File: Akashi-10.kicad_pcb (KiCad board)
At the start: 2 copper layers, 66 x 65 mm, 12 parts, among them J1 Conn_02x20_Odd_Even, P1 EL-210-KEY, U1 9-ST-20

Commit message: Fixed name of the KEY matrix sisgnal.
The Row signal order was up-side-down. Fixed.
The Col signal was 1 origin. Fixed as 0 origin.
Sylscreen modfified.
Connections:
- J1 pad 30: Net-(J1-Pad30) -> unconnected-(J1-Pad30)
- J1 pad 32: Net-(J1-Pad32) -> unconnected-(J1-Pad32)
- J1 pad 34: Net-(J1-Pad34) -> unconnected-(J1-Pad34)
- J1 pad 36: Net-(J1-Pad36) -> unconnected-(J1-Pad36)
- J1 pad 39: Net-(J1-Pad39) -> unconnected-(J1-Pad39)
- J1 pad 4: Net-(J1-Pad4) -> unconnected-(J1-Pad4)
- P1 pad 12: Net-(P1-Pad12) -> unconnected-(P1-Pad12)
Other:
- net class Default removed
- board text added: "Akashi-10 v1.0.3"
- board text removed: "Akashi-10 v1.0.2"

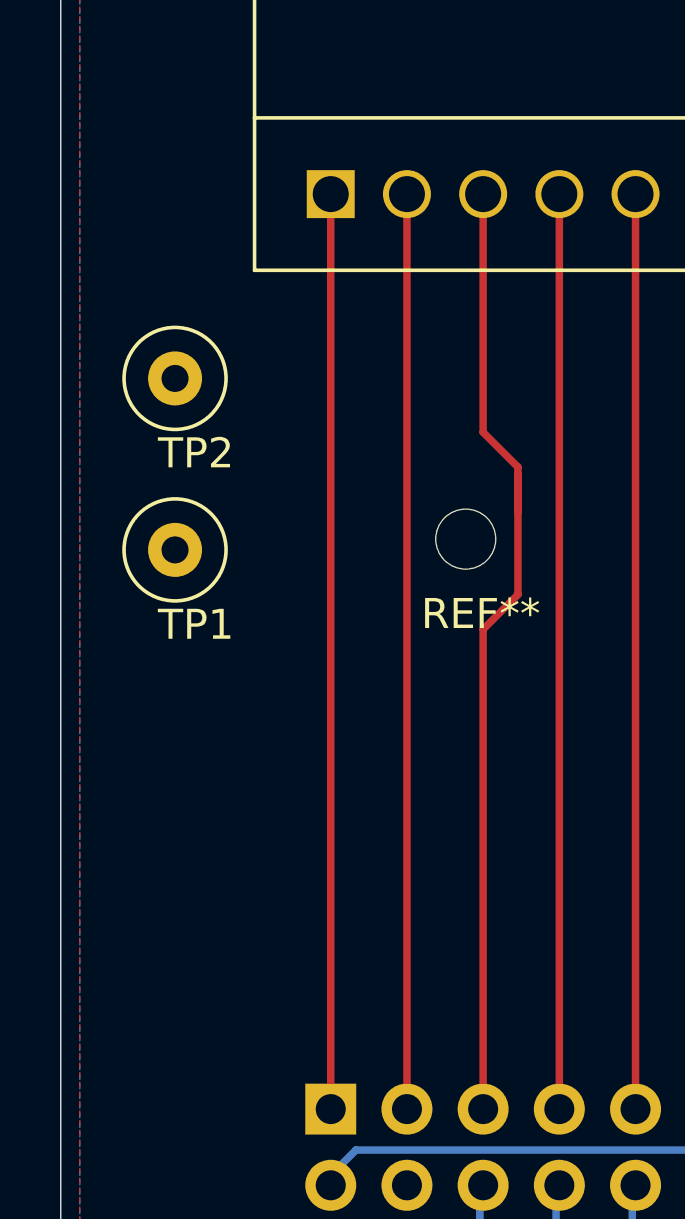
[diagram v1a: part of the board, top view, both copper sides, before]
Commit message: Add pin 1 mark to the connector.
Add pin 1 mark to the connector of the layout.
Movied Testpoint ( 3.3 and GND hole )
Update photo.
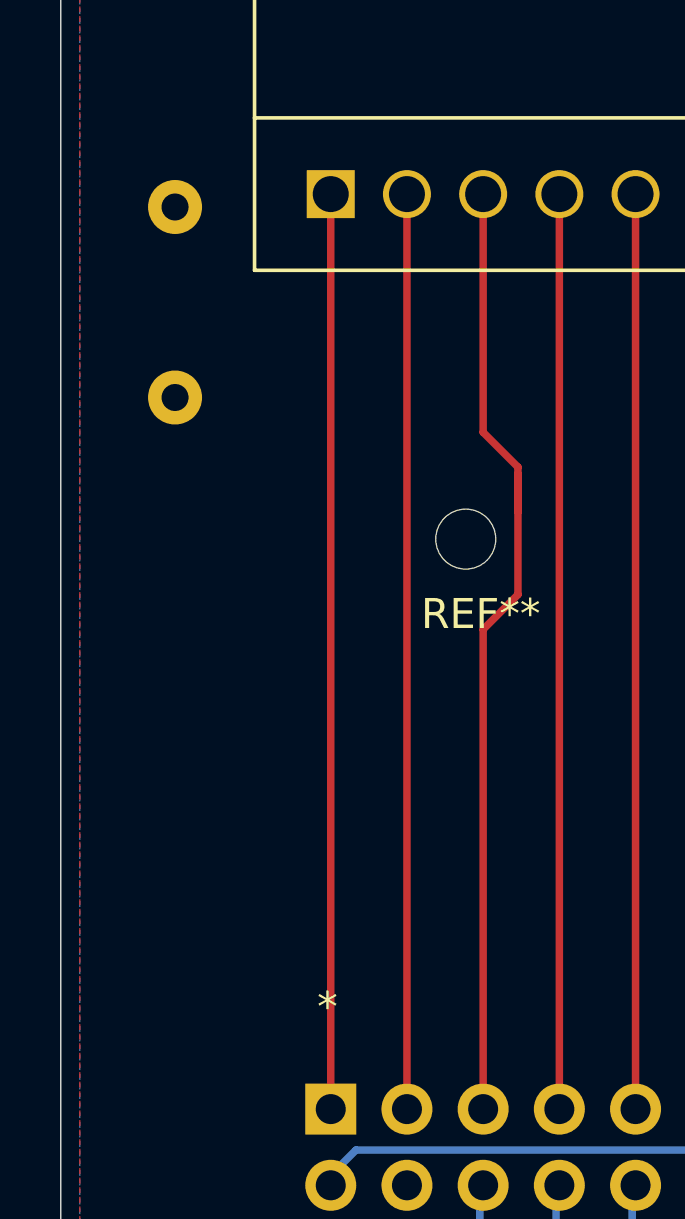
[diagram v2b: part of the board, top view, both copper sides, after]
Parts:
- TP1, TP2: moved to B.Cu
- moved TP2 5.71 mm to (122.8, 85.9), turned to 180 degrees
- moved TP1 5.08 mm to (122.8, 92.3), turned to 180 degrees
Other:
- board text added: "*"
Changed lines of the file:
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@@
       (net 1 "GND") (pinfunction "GND") (pintype "power_in"))
-  )
-  (footprint "TestPoint:TestPoint_Loop_D2.60mm_Drill0.9mm_Beaded" (layer "F.Cu")
-    (at 122.81 97.36)
-    (descr "wire loop with bead as test point, loop diameter2.6mm, hole diameter 0.9mm")
-    (tags "test point wire loop bead")
-    (property "Sheetfile" "Akashi-10.kicad_sch")
-    (property "Sheetname" "")
-    (attr through_hole)
-    (fp_text reference "TP1" (at 0.7 2.5) (layer "F.SilkS")
-      (effects (font (size 1 1) (thickness 0.15)))
-    )
-    (fp_text value "TestPoint" (at 0 -2.8) (layer "F.Fab")
-      (effects (font (size 1 1) (thickness 0.15)))
-    )
-    (fp_text user "${REFERENCE}" (at 0.7 2.5) (layer "F.Fab")
-      (effects (font (size 1 1) (thickness 0.15)))
-    )
-    (fp_circle (center 0 0) (end 1.7 0) (layer "F.SilkS") (width 0.12) (fill none))
-    (fp_circle (center 0 0) (end 2 0) (layer "F.CrtYd") (width 0.05) (fill none))
-    (fp_line (start 1.3 0.3) (end 1.3 -0.3) (layer "F.Fab") (width 0.12))
-    (fp_line (start -1.3 -0.3) (end -1.3 0.3) (layer "F.Fab") (width 0.12))
-    (fp_line (start 1.3 -0.3) (end -1.3 -0.3) (layer "F.Fab") (width 0.12))
-    (fp_line (start -1.3 0.3) (end 1.3 0.3) (layer "F.Fab") (width 0.12))
-    (fp_circle (center 0 0) (end 1.5 0) (layer "F.Fab") (width 0.12) (fill none))
-    (pad "1" thru_hole circle locked (at 0 0) (size 1.8 1.8) (drill 0.9) (layers *.Cu *.Mask)
-      (net 1 "GND") (pinfunction "1") (pintype "passive"))
-    (model "${KISYS3DMOD}/TestPoint.3dshapes/TestPoint_Loop_D2.60mm_Drill0.9mm_Beaded.wrl"
-      (offset (xyz 0 0 0))
-      (scale (xyz 1 1 1))
-      (rotate (xyz 0 0 0))
-    )
-  )
-  (footprint "TestPoint:TestPoint_Loop_D2.60mm_Drill0.9mm_Beaded" (layer "F.Cu")
-    (at 122.81 91.645)
-    (descr "wire loop with bead as test point, loop diameter2.6mm, hole diameter 0.9mm")
-    (tags "test point wire loop bead")
-    (property "Sheetfile" "Akashi-10.kicad_sch")
-    (property "Sheetname" "")
-    (attr through_hole)
-    (fp_text reference "TP2" (at 0.7 2.5) (layer "F.SilkS")
-      (effects (font (size 1 1) (thickness 0.15)))
-    )
-    (fp_text value "TestPoint" (at 0 -2.8) (layer "F.Fab")
-      (effects (font (size 1 1) (thickness 0.15)))
-    )
-    (fp_text user "${REFERENCE}" (at 0.7 2.5) (layer "F.Fab")
-      (effects (font (size 1 1) (thickness 0.15)))
-    )
-    (fp_circle (center 0 0) (end 1.7 0) (layer "F.SilkS") (width 0.12) (fill none))
-    (fp_circle (center 0 0) (end 2 0) (layer "F.CrtYd") (width 0.05) (fill none))
-    (fp_line (start 1.3 -0.3) (end -1.3 -0.3) (layer "F.Fab") (width 0.12))
-    (fp_line (start -1.3 0.3) (end 1.3 0.3) (layer "F.Fab") (width 0.12))
-    (fp_line (start 1.3 0.3) (end 1.3 -0.3) (layer "F.Fab") (width 0.12))
-    (fp_line (start -1.3 -0.3) (end -1.3 0.3) (layer "F.Fab") (width 0.12))
-    (fp_circle (center 0 0) (end 1.5 0) (layer "F.Fab") (width 0.12) (fill none))
-    (pad "1" thru_hole circle locked (at 0 0) (size 1.8 1.8) (drill 0.9) (layers *.Cu *.Mask)
-      (net 3 "+3V3") (pinfunction "1") (pintype "passive"))
-    (model "${KISYS3DMOD}/TestPoint.3dshapes/TestPoint_Loop_D2.60mm_Drill0.9mm_Beaded.wrl"
-      (offset (xyz 0 0 0))
-      (scale (xyz 1 1 1))
-      (rotate (xyz 0 0 0))
-    )
   )
   (footprint "9-ST-20:9-ST-20" (layer "F.Cu")
@@
     )
     (pad "" np_thru_hole circle locked (at 0 0) (size 2.8 2.8) (drill 2.8) (layers *.Cu *.Mask))
+  )
+  (footprint "TestPoint:TestPoint_Loop_D2.60mm_Drill0.9mm_Beaded" (layer "B.Cu")
+    (at 122.81 92.28 180)
+    (descr "wire loop with bead as test point, loop diameter2.6mm, hole diameter 0.9mm")
+    (tags "test point wire loop bead")
+    (property "Sheetfile" "Akashi-10.kicad_sch")
+    (property "Sheetname" "")
+    (attr through_hole)
+    (fp_text reference "TP1" (at 0.7 -2.5) (layer "B.SilkS")
+      (effects (font (size 1 1) (thickness 0.15)) (justify mirror))
+    )
+    (fp_text value "TestPoint" (at 0 2.8) (layer "B.Fab")
+      (effects (font (size 1 1) (thickness 0.15)) (justify mirror))
+    )
+    (fp_text user "${REFERENCE}" (at 0.7 -2.5) (layer "B.Fab")
+      (effects (font (size 1 1) (thickness 0.15)) (justify mirror))
+    )
+    (fp_circle (center 0 0) (end 1.7 0) (layer "B.SilkS") (width 0.12) (fill none))
+    (fp_circle (center 0 0) (end 2 0) (layer "B.CrtYd") (width 0.05) (fill none))
+    (fp_line (start 1.3 -0.3) (end 1.3 0.3) (layer "B.Fab") (width 0.12))
+    (fp_line (start -1.3 0.3) (end -1.3 -0.3) (layer "B.Fab") (width 0.12))
+    (fp_line (start 1.3 0.3) (end -1.3 0.3) (layer "B.Fab") (width 0.12))
+    (fp_line (start -1.3 -0.3) (end 1.3 -0.3) (layer "B.Fab") (width 0.12))
+    (fp_circle (center 0 0) (end 1.5 0) (layer "B.Fab") (width 0.12) (fill none))
+    (pad "1" thru_hole circle locked (at 0 0 180) (size 1.8 1.8) (drill 0.9) (layers *.Cu *.Mask)
+      (net 1 "GND") (pinfunction "1") (pintype "passive"))
+    (model "${KISYS3DMOD}/TestPoint.3dshapes/TestPoint_Loop_D2.60mm_Drill0.9mm_Beaded.wrl"
+      (offset (xyz 0 0 0))
+      (scale (xyz 1 1 1))
+      (rotate (xyz 0 0 0))
+    )
+  )
+  (footprint "TestPoint:TestPoint_Loop_D2.60mm_Drill0.9mm_Beaded" (layer "B.Cu")
+    (at 122.81 85.93 180)
+    (descr "wire loop with bead as test point, loop diameter2.6mm, hole diameter 0.9mm")
+    (tags "test point wire loop bead")
+    (property "Sheetfile" "Akashi-10.kicad_sch")
+    (property "Sheetname" "")
+    (attr through_hole)
+    (fp_text reference "TP2" (at 0.7 -2.5) (layer "B.SilkS")
+      (effects (font (size 1 1) (thickness 0.15)) (justify mirror))
+    )
+    (fp_text value "TestPoint" (at 0 2.8) (layer "B.Fab")
+      (effects (font (size 1 1) (thickness 0.15)) (justify mirror))
+    )
+    (fp_text user "${REFERENCE}" (at 0.7 -2.5) (layer "B.Fab")
+      (effects (font (size 1 1) (thickness 0.15)) (justify mirror))
+    )
+    (fp_circle (center 0 0) (end 1.7 0) (layer "B.SilkS") (width 0.12) (fill none))
+    (fp_circle (center 0 0) (end 2 0) (layer "B.CrtYd") (width 0.05) (fill none))
+    (fp_line (start 1.3 0.3) (end -1.3 0.3) (layer "B.Fab") (width 0.12))
+    (fp_line (start -1.3 -0.3) (end 1.3 -0.3) (layer "B.Fab") (width 0.12))
+    (fp_line (start 1.3 -0.3) (end 1.3 0.3) (layer "B.Fab") (width 0.12))
+    (fp_line (start -1.3 0.3) (end -1.3 -0.3) (layer "B.Fab") (width 0.12))
+    (fp_circle (center 0 0) (end 1.5 0) (layer "B.Fab") (width 0.12) (fill none))
+    (pad "1" thru_hole circle locked (at 0 0 180) (size 1.8 1.8) (drill 0.9) (layers *.Cu *.Mask)
+      (net 3 "+3V3") (pinfunction "1") (pintype "passive"))
+    (model "${KISYS3DMOD}/TestPoint.3dshapes/TestPoint_Loop_D2.60mm_Drill0.9mm_Beaded.wrl"
+      (offset (xyz 0 0 0))
+      (scale (xyz 1 1 1))
+      (rotate (xyz 0 0 0))
+    )
   )
   (footprint "Connector_PinHeader_2.54mm:PinHeader_2x20_P2.54mm_Vertical" (layer "B.Cu")
@@
     (effects (font (size 1 1) (thickness 0.2)) (justify mirror))
   )
-  (gr_text "GND" (at 127.889991 97.360003) (layer "B.SilkS")
+  (gr_text "GND" (at 122.81 97.360003) (layer "B.SilkS")
     (effects (font (size 1.5 1.5) (thickness 0.3)) (justify mirror))
   )
@@
     (effects (font (size 1.5 1.5) (thickness 0.3)) (justify mirror))
   )
-  (gr_text "3.3v" (at 127.89 92.28) (layer "B.SilkS")
+  (gr_text "3.3v" (at 122.81 82.12) (layer "B.SilkS")
     (effects (font (size 1.5 1.5) (thickness 0.3)) (justify mirror))
   )
+  (gr_text "*" (at 127.89 112.6) (layer "F.SilkS")
+    (effects (font (size 1 1) (thickness 0.15)))
+  )
   (segment (start 130 134.5) (end 130 127.41) (width 0.25) (layer "B.Cu") (net 1))
